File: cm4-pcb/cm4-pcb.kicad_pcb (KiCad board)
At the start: 2 copper layers, 140 x 70.5 mm, 43 parts, among them J1 Conn_01x02_Pin, J2 Conn_01x02_Pin, J3 USB1125-GF-B, J4 Conn_02x03_Odd_Even, J5 Conn_01x04, J6 J0011D21NL, J7 Conn_01x02, J8 Conn_01x02, J9 Conn_01x02_Pin, U1 Pfostenstecker_6_2x3, U2 Pfostenstecker_6_2x3, U3 ESD122DMYR, U4 ESD122DMYR, U5 SMD-PUSH-BTN, U6 ESD122DMYR, U7 ESD122DMYR

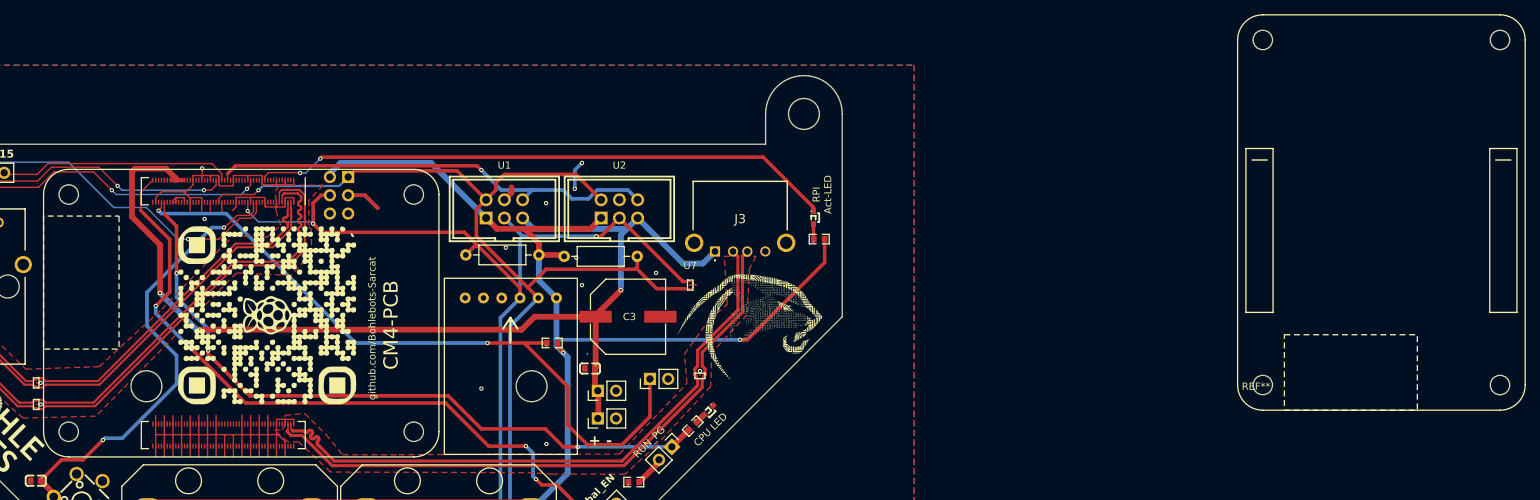
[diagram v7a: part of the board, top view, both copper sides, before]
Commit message: Fixed connections for cm4 connectors
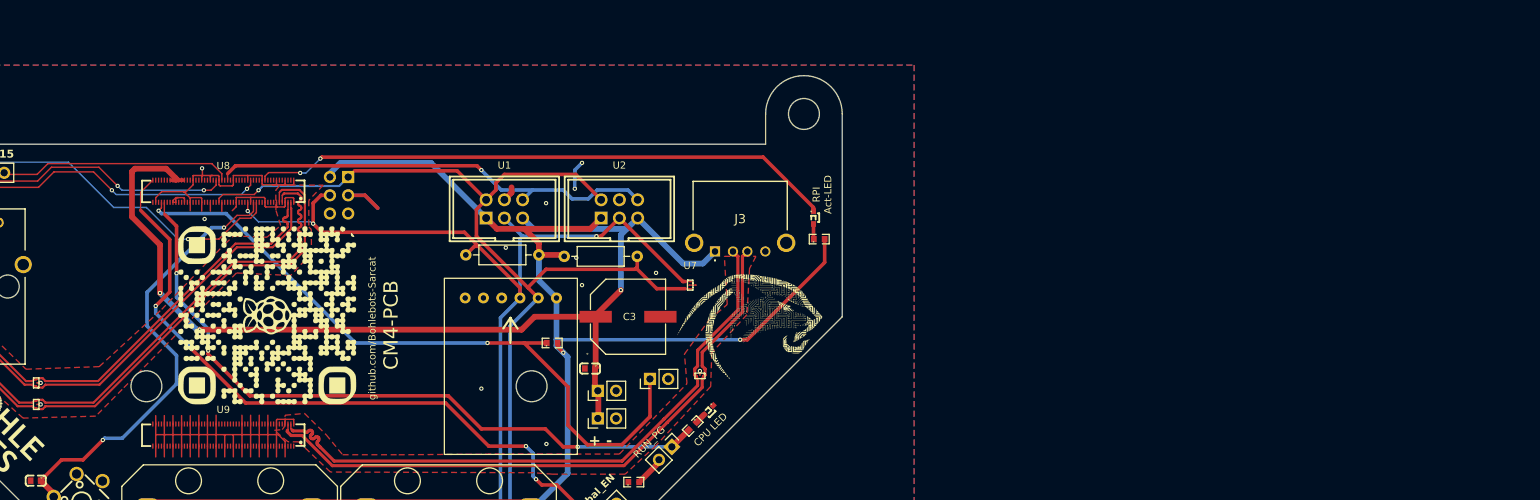
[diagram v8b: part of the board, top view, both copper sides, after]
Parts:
- removed Module1: ComputeModule4-CM4, CM4IO:Raspberry-Pi-4-Compute-Module
- removed REF**: CM4-sarcat, sarcat:CM4-sarcat
- added U8: DF40HC(3_0)-100DS-0_4V(51), BohleBots:CONN-SMD_DF40HC-3.0-100DS-0.4V-51, F.Cu at (-16.1, 37.5)
- added U9: DF40HC(3_0)-100DS-0_4V(51), BohleBots:CONN-SMD_DF40HC-3.0-100DS-0.4V-51, F.Cu at (-16.1, 71.5)
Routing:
- net Net-(Module1A-GPIO_VREF(1.8v/3.3v_Input)): track 3.90 -> 0.00 mm
- net (no net): track 0.00 -> 3.90 mm
